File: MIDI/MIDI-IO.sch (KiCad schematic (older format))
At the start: 17 parts, among them IC2 6N138, P3 DIN_5, P4 DIN_5, P5 DIN_5, Q1 BC557, Q2 BC557

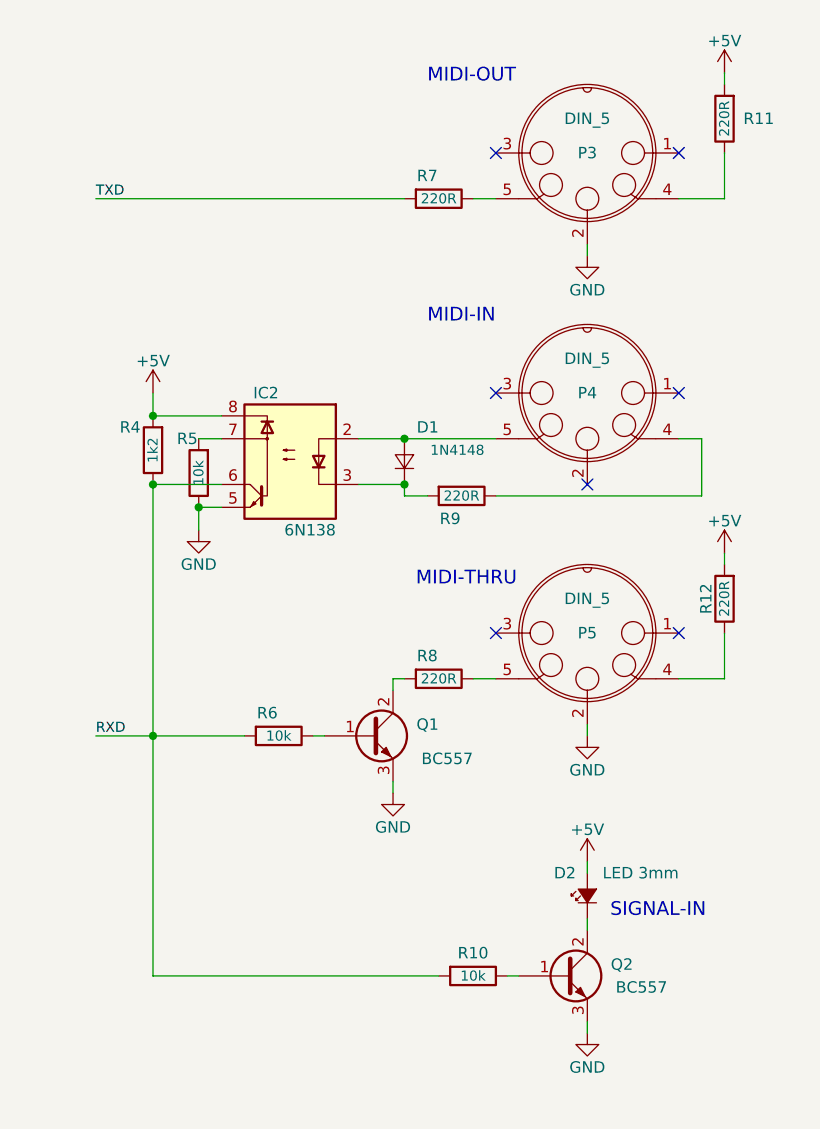
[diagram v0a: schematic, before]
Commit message: Wrong pinout for MIDI-IN
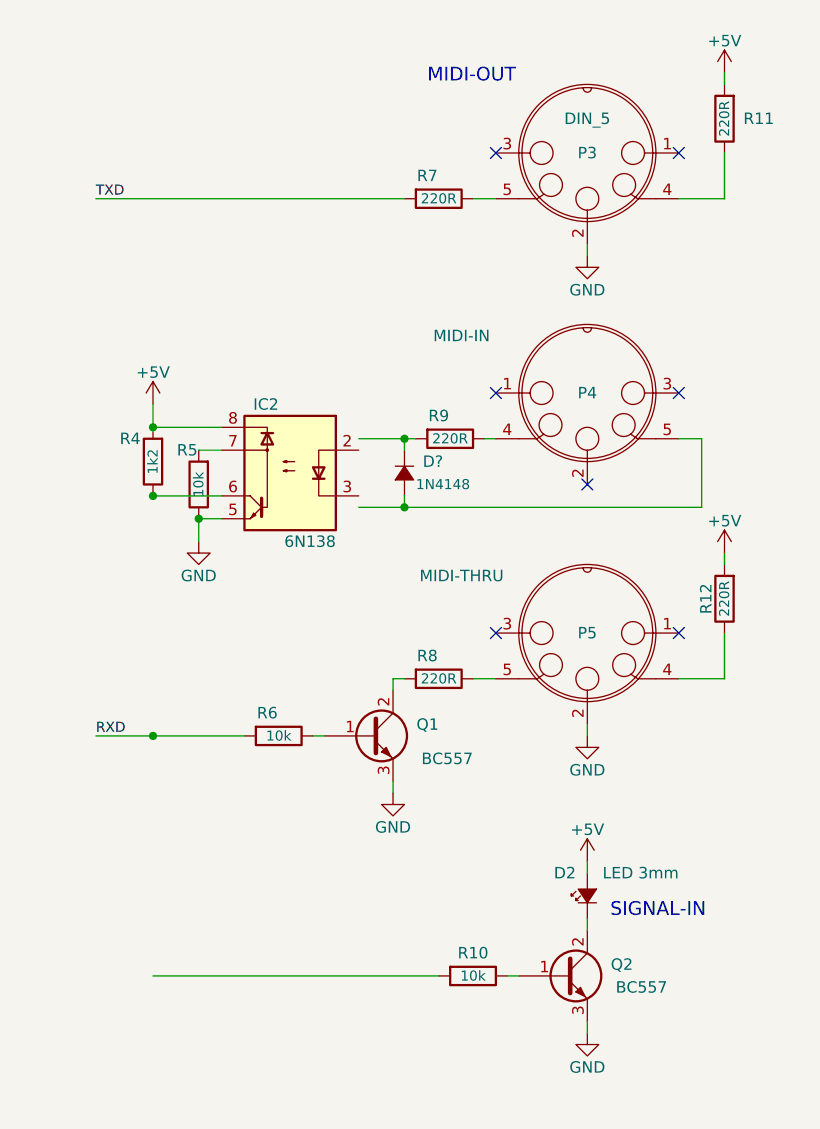
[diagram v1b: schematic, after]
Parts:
- removed D1: 1N4148, Diodes_ThroughHole:Diode_DO-35_SOD27_Horizontal_RM10, symbol D_Small
- added D?: 1N4148, symbol D_Small_ALT
- P4: value DIN_5 -> MIDI-IN
- P5: value DIN_5 -> MIDI-THRU
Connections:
- wire segments 35 -> 34
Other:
- note removed: "MIDI-IN"
- note removed: "MIDI-THRU"
- moved on the sheet: IC2, R4, R5, R9
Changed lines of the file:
@@
 L 6N136 IC2
 U 1 1 572B426E
-P 8050 3450
-F 0 "IC2" H 8100 3750 50  0000 L CNN
-F 1 "6N138" H 7850 3150 50  0000 L CNN
-F 2 "Housings_DIP:DIP-8_W7.62mm_LongPads" H 7850 3150 50  0001 L CIN
-F 3 "" H 8050 3450 50  0000 L CNN
-	1    8050 3450
+P 8050 3500
+F 0 "IC2" H 8100 3800 50  0000 L CNN
+F 1 "6N138" H 7850 3200 50  0000 L CNN
+F 2 "Housings_DIP:DIP-8_W7.62mm_LongPads" H 7850 3200 50  0001 L CIN
+F 3 "" H 8050 3500 50  0000 L CNN
+	1    8050 3500
 	-1   0    0    -1
 $EndComp
@@
 L R R9
 U 1 1 572B4E06
-P 8800 3600
-F 0 "R9" V 8900 3550 50  0000 C CNN
-F 1 "220R" V 8800 3600 44  0000 C CNN
-F 2 "Resistors_SMD:R_1206_HandSoldering" V 8730 3600 50  0001 C CNN
-F 3 "" H 8800 3600 50  0000 C CNN
-	1    8800 3600
+P 8750 3350
+F 0 "R9" V 8650 3300 50  0000 C CNN
+F 1 "220R" V 8750 3350 44  0000 C CNN
+F 2 "Resistors_SMD:R_1206_HandSoldering" V 8680 3350 50  0001 C CNN
+F 3 "" H 8750 3350 50  0000 C CNN
+	1    8750 3350
 	0    1    1    0
 $EndComp
@@
 L R R4
 U 1 1 572B4E5A
-P 7450 3400
-F 0 "R4" H 7550 3300 50  0000 C CNN
-F 1 "1k2" V 7450 3400 44  0000 C CNN
-F 2 "Resistors_SMD:R_1206_HandSoldering" V 7380 3400 50  0001 C CNN
-F 3 "" H 7450 3400 50  0000 C CNN
-	1    7450 3400
+P 7450 3450
+F 0 "R4" H 7550 3350 50  0000 C CNN
+F 1 "1k2" V 7450 3450 44  0000 C CNN
+F 2 "Resistors_SMD:R_1206_HandSoldering" V 7380 3450 50  0001 C CNN
+F 3 "" H 7450 3450 50  0000 C CNN
+	1    7450 3450
 	-1   0    0    1
 $EndComp
@@
 L +5V #PWR016
 U 1 1 572B513E
-P 7450 3150
-F 0 "#PWR016" H 7450 3000 50  0001 C CNN
-F 1 "+5V" H 7450 3290 50  0000 C CNN
-F 2 "" H 7450 3150 60  0000 C CNN
-F 3 "" H 7450 3150 60  0000 C CNN
-	1    7450 3150
+P 7450 3200
+F 0 "#PWR016" H 7450 3050 50  0001 C CNN
+F 1 "+5V" H 7450 3340 50  0000 C CNN
+F 2 "" H 7450 3200 60  0000 C CNN
+F 3 "" H 7450 3200 60  0000 C CNN
+	1    7450 3200
 	1    0    0    -1
 $EndComp
@@
 L GND #PWR017
 U 1 1 572B5678
-P 7650 3750
-F 0 "#PWR017" H 7650 3500 50  0001 C CNN
-F 1 "GND" H 7650 3600 50  0000 C CNN
-F 2 "" H 7650 3750 50  0000 C CNN
-F 3 "" H 7650 3750 50  0000 C CNN
-	1    7650 3750
+P 7650 3800
+F 0 "#PWR017" H 7650 3550 50  0001 C CNN
+F 1 "GND" H 7650 3650 50  0000 C CNN
+F 2 "" H 7650 3800 50  0000 C CNN
+F 3 "" H 7650 3800 50  0000 C CNN
+	1    7650 3800
 	1    0    0    -1
 $EndComp
@@
 L R R5
 U 1 1 572B597E
-P 7650 3500
-F 0 "R5" H 7700 3350 50  0000 C CNN
-F 1 "10k" V 7650 3500 44  0000 C CNN
-F 2 "Resistors_SMD:R_1206_HandSoldering" V 7580 3500 50  0001 C CNN
-F 3 "" H 7650 3500 50  0000 C CNN
-	1    7650 3500
+P 7650 3550
+F 0 "R5" H 7700 3400 50  0000 C CNN
+F 1 "10k" V 7650 3550 44  0000 C CNN
+F 2 "Resistors_SMD:R_1206_HandSoldering" V 7580 3550 50  0001 C CNN
+F 3 "" H 7650 3550 50  0000 C CNN
+	1    7650 3550
 	-1   0    0    1
 $EndComp
@@
 P 9350 3150
 F 0 "P4" H 9350 3150 50  0000 C CNN
-F 1 "DIN_5" H 9350 3000 50  0000 C CNN
+F 1 "MIDI-IN" H 8800 2900 50  0000 C CNN
 F 2 "" H 9350 3150 50  0001 C CNN
 F 3 "" H 9350 3150 50  0000 C CNN
 	1    9350 3150
-	-1   0    0    1
-$EndComp
-$Comp
-L D_Small D1
-U 1 1 572B42B2
-P 8550 3450
-F 0 "D1" V 8700 3300 50  0000 L CNN
-F 1 "1N4148" V 8600 3100 44  0000 L CNN
-F 2 "Diodes_ThroughHole:Diode_DO-35_SOD27_Horizontal_RM10" V 8550 3450 50  0001 C CNN
-F 3 "" V 8550 3450 50  0000 C CNN
-	1    8550 3450
-	0    -1   -1   0
+	1    0    0    1
 $EndComp
 NoConn ~ 9350 3550
@@
 P 9350 4200
 F 0 "P5" H 9350 4200 50  0000 C CNN
-F 1 "DIN_5" H 9350 4050 50  0000 C CNN
+F 1 "MIDI-THRU" H 9900 3950 50  0000 C CNN
 F 2 "" H 9350 4200 50  0001 C CNN
 F 3 "" H 9350 4200 50  0000 C CNN
@@
 	7200 2300 8550 2300
 Wire Wire Line
-	7650 3750 7650 3650
-Wire Wire Line
-	7650 3650 7750 3650
-Wire Wire Line
-	7750 3350 7650 3350
-Wire Wire Line
-	7450 3250 7750 3250
-Wire Wire Line
-	7450 3150 7450 3250
-Connection ~ 7450 3550
-Connection ~ 7450 3250
-Connection ~ 7650 3650
-Wire Wire Line
-	8350 3350 8950 3350
+	7650 3800 7650 3700
+Wire Wire Line
+	7650 3700 7750 3700
+Wire Wire Line
+	7750 3400 7650 3400
+Wire Wire Line
+	7450 3300 7750 3300
+Wire Wire Line
+	7450 3200 7450 3300
+Connection ~ 7450 3600
+Connection ~ 7450 3300
+Connection ~ 7650 3700
 Wire Wire Line
 	9750 3350 9850 3350
-Wire Wire Line
-	9850 3350 9850 3600
-Wire Wire Line
-	9850 3600 8950 3600
-Wire Wire Line
-	8350 3550 8550 3550
-Wire Wire Line
-	8550 3550 8550 3600
-Wire Wire Line
-	8550 3600 8650 3600
-Connection ~ 8550 3550
 Connection ~ 8550 3350
 Wire Wire Line
@@
 Wire Wire Line
 	9950 3850 9950 3900
-Wire Wire Line
-	7450 3550 7450 5700
 Wire Wire Line
 	7450 5700 8700 5700
@@
 RXD
 Wire Wire Line
-	7750 3550 7450 3550
+	7750 3600 7450 3600
 Text Notes 8650 1800 0    60   ~ 0
 MIDI-OUT
-Text Notes 8650 2850 0    60   ~ 0
-MIDI-IN
-Text Notes 8600 4000 0    60   ~ 0
-MIDI-THRU
 Text Notes 9450 5450 0    60   ~ 0
 SIGNAL-IN
+Wire Wire Line
+	8350 3650 9850 3650
+Wire Wire Line
+	9850 3650 9850 3350
+Wire Wire Line
+	8900 3350 8950 3350
+Wire Wire Line
+	8350 3350 8600 3350
+$Comp
+L D_Small_ALT D?
+U 1 1 5B54592C
+P 8550 3500
+F 0 "D?" V 8500 3580 50  0000 L CNN
+F 1 "1N4148" V 8600 3550 44  0000 L CNN
+F 2 "" V 8550 3500 50  0001 C CNN
+F 3 "" V 8550 3500 50  0001 C CNN
+	1    8550 3500
+	0    1    1    0
+$EndComp
+Wire Wire Line
+	8550 3400 8550 3350
+Wire Wire Line
+	8550 3600 8550 3650
+Connection ~ 8550 3650
 $EndSCHEMATC

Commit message: Update to KiCad 5
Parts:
- removed D2: LED 3mm, symbol Led_Small
- removed D?: 1N4148, symbol D_Small_ALT
- removed IC2: 6N138, Housings_DIP:DIP-8_W7.62mm_LongPads, symbol 6N136
- removed P3: DIN_5, symbol DIN_5
- removed P4: MIDI-IN, symbol DIN_5
- removed P5: MIDI-THRU, symbol DIN_5
- removed Q1, Q2: BC557, symbol Q_NPN_BCE
- removed R10, R5, R6: 10k, Resistors_SMD:R_1206_HandSoldering, symbol R
- removed R11, R12, R7, R8, R9: 220R, Resistors_SMD:R_1206_HandSoldering, symbol R
- removed R4: 1k2, Resistors_SMD:R_1206_HandSoldering, symbol R
- added D?: DUS, symbol Device:D_Small_ALT
- added D?: LED3MM, symbol Device:LED_Small_ALT
- added J? (x2): MIDI-IN, symbol Connector:DIN-5_180degree
- added J?: MIDI-OUT, symbol Connector:DIN-5_180degree
- added Q? (x2): BC547, Package_TO_SOT_THT:TO-92_Inline, symbol Transistor_BJT:BC547
- added R? (x5): 220R, symbol Device:R_Small
- added R? (x3): 10k, symbol Device:R_Small
- added R?: 1k2, symbol Device:R_Small
- added U?: 6N136, Package_DIP:DIP-8_W7.62mm, symbol Isolator:6N136
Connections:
- wire segments 34 -> 40
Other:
- note removed: "MIDI-OUT"
